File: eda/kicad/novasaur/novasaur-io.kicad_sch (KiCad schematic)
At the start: 77 parts, among them J1 POWER IN, J10 EXPANSION, J2 KEYBOARD, J3 SERIAL, J4 DISPLAY, J5 GPU OUT, J6 AUDIO OUT, J7 EXPANSION, J8 EXPANSION, J9 EXPANSION, Q1 2N3904, Q2 2N3904, Q3 2N3904, SW1 POWER, U1 74F86, U2 74F32, U3 74F11, U38 CD4053, U39 MAX232, U4 74F139, U40 NJM4580, U41 BA50DD0WT, U5 74F139

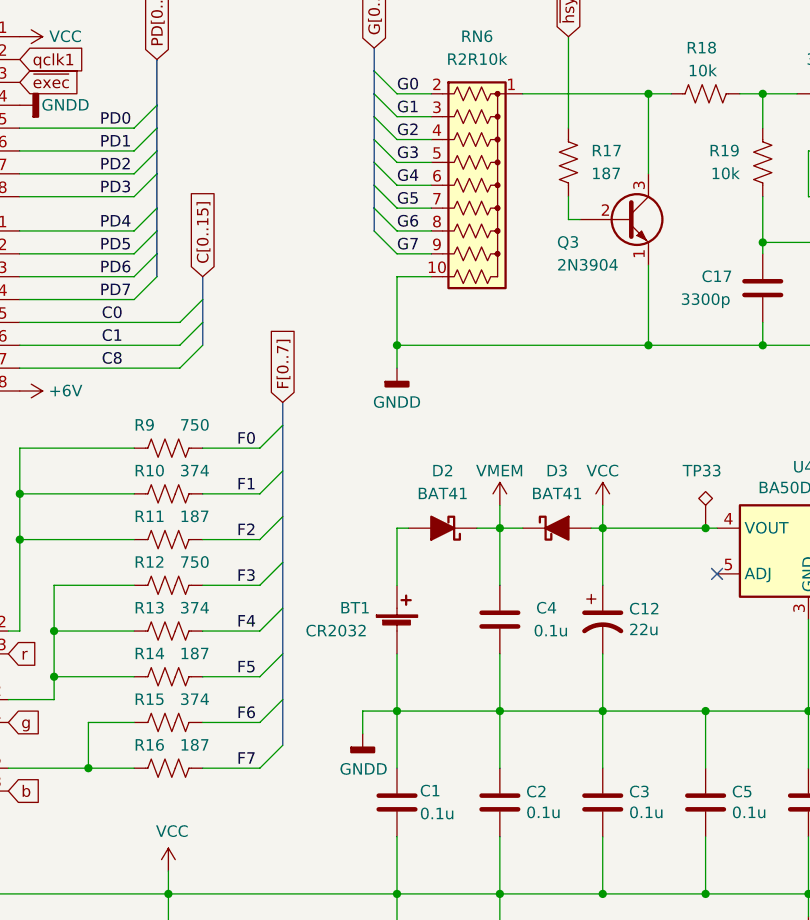
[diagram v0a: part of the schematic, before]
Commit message: Schematic updates
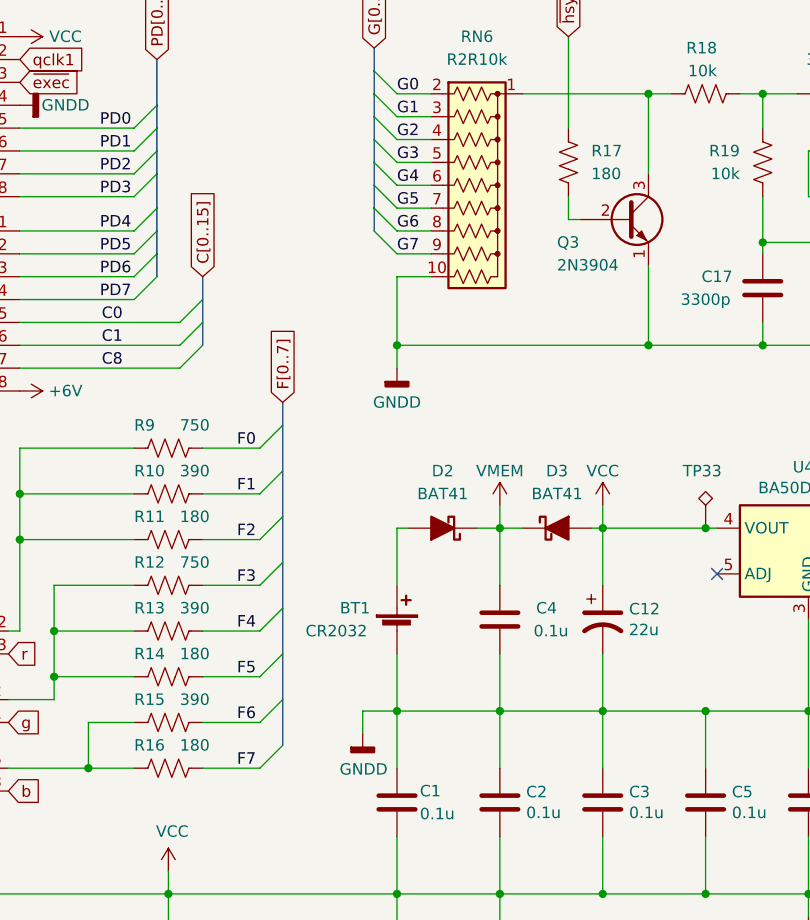
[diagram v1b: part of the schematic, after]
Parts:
- R10, R13, R15: value 374 -> 390
- R11, R14, R16, R17: value 187 -> 180
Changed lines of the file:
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@@
   (title_block
     (title "Input/Output")
-    (date "2022-03-14")
+    (date "2022-08-07")
     (rev "1.10")
     (comment 1 "(c) Solid State Machines 2022")
@@
       (effects (font (size 1.27 1.27)) (justify left))
     )
-    (property "Value" "187" (id 1) (at 158.75 46.99 0)
+    (property "Value" "180" (id 1) (at 158.75 46.99 0)
       (effects (font (size 1.27 1.27)) (justify left))
     )
@@
       (effects (font (size 1.27 1.27)) (justify left))
     )
-    (property "Value" "187" (id 1) (at 113.03 110.49 90)
+    (property "Value" "180" (id 1) (at 113.03 110.49 90)
       (effects (font (size 1.27 1.27)) (justify left))
     )
@@
       (effects (font (size 1.27 1.27)) (justify left))
     )
-    (property "Value" "187" (id 1) (at 113.03 100.33 90)
+    (property "Value" "180" (id 1) (at 113.03 100.33 90)
       (effects (font (size 1.27 1.27)) (justify left))
     )
@@
       (effects (font (size 1.27 1.27)) (justify left))
     )
-    (property "Value" "187" (id 1) (at 113.03 85.09 90)
+    (property "Value" "180" (id 1) (at 113.03 85.09 90)
       (effects (font (size 1.27 1.27)) (justify left))
     )
@@
       (effects (font (size 1.27 1.27)) (justify left))
     )
-    (property "Value" "374" (id 1) (at 113.03 105.41 90)
+    (property "Value" "390" (id 1) (at 113.03 105.41 90)
       (effects (font (size 1.27 1.27)) (justify left))
     )
@@
       (effects (font (size 1.27 1.27)) (justify left))
     )
-    (property "Value" "374" (id 1) (at 113.03 95.25 90)
+    (property "Value" "390" (id 1) (at 113.03 95.25 90)
       (effects (font (size 1.27 1.27)) (justify left))
     )
@@
       (effects (font (size 1.27 1.27)) (justify left))
     )
-    (property "Value" "374" (id 1) (at 113.03 80.01 90)
-      (effects (font (size 1.27 1.27)) (justify left))
-    )
+    (property "Value" "390" (id 1) (at 113.03 80.01 90)
+      (effects (font (size 1.27 1.27)) (justify left))
+    )
